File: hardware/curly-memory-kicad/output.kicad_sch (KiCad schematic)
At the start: 37 parts

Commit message: schematic updated with component fields on more components
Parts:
- C? (x12): footprint (none) -> Capacitor_SMD:C_0805_2012Metric_Pad1.18x1.45mm_HandSolder
- J? (x4): footprint (none) -> AudioJacks:Jack_3.5mm_QingPu_WQP-PJ398SM_Vertical
- R? (x12): footprint Resistor_THT:R_Axial_DIN0309_L9.0mm_D3.2mm_P12.70mm_Horizontal -> Resistor_SMD:R_0805_2012Metric_Pad1.20x1.40mm_HandSolder

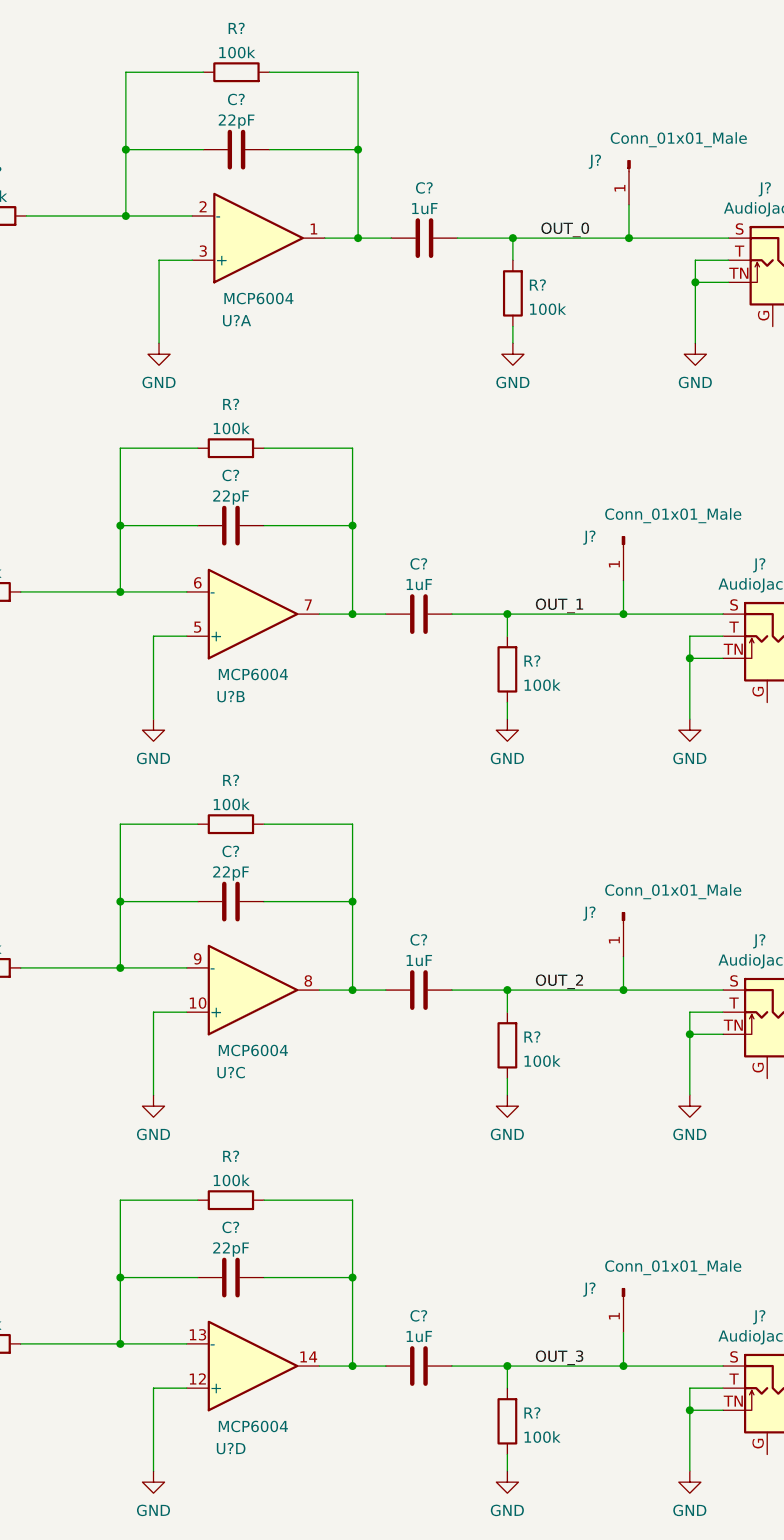
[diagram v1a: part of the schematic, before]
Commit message: all components have part numbers
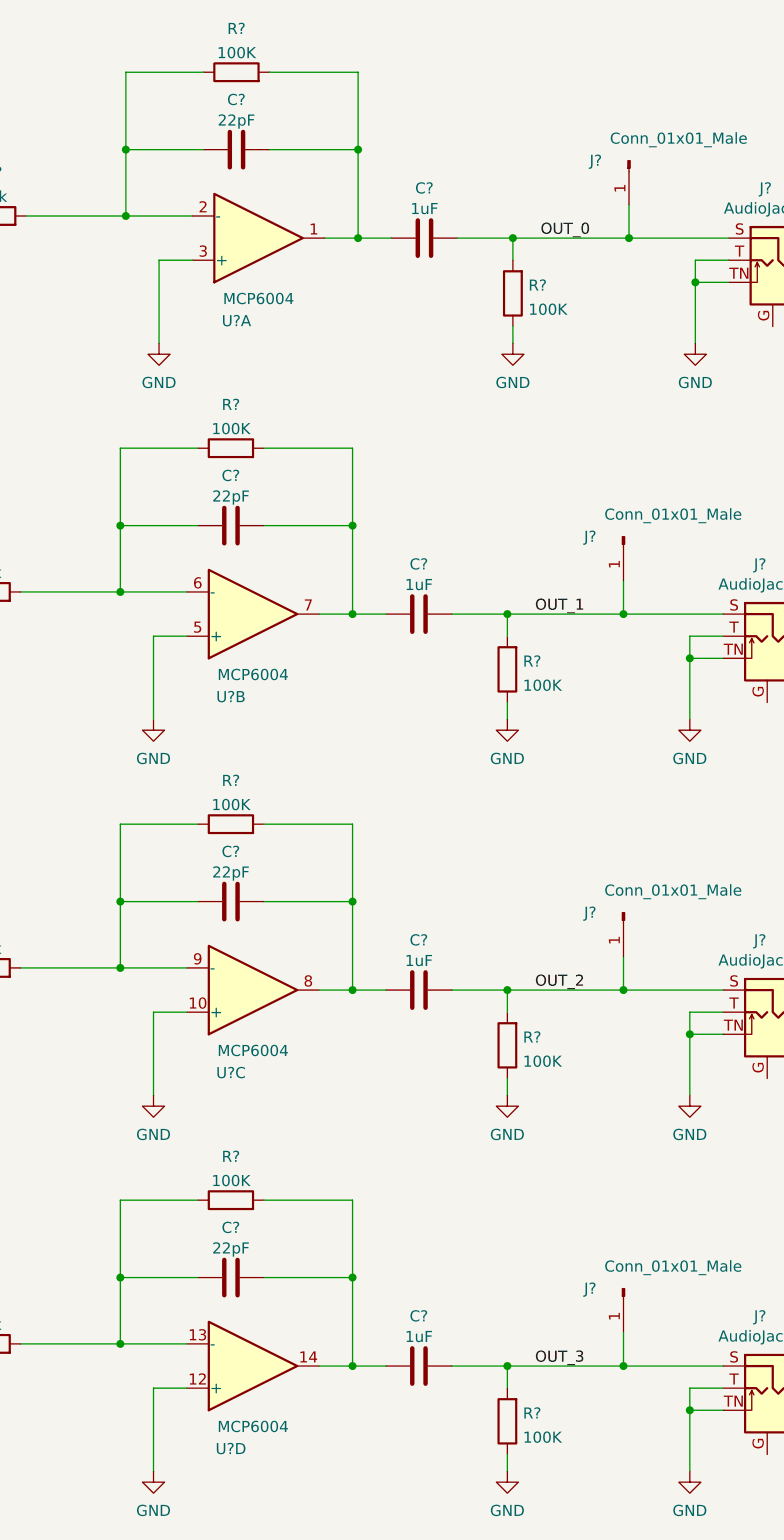
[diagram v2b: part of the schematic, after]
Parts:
- R? (x8): value 100k -> 100K
- U? (x5): footprint (none) -> Package_SO:SOIC-14_3.9x8.7mm_P1.27mm
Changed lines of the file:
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@@
     (in_bom yes) (on_board yes) (fields_autoplaced)
     (property "Reference" "R?" (id 0) (at 73.66 105.5075 90))
-    (property "Value" "100k" (id 1) (at 73.66 108.2826 90))
+    (property "Value" "100K" (id 1) (at 73.66 108.2826 90))
     (property "Footprint" "Resistor_SMD:R_0805_2012Metric_Pad1.20x1.40mm_HandSolder" (id 2) (at 73.66 112.268 90)
       (effects (font (size 1.27 1.27)) hide)
@@
       (effects (font (size 1.27 1.27)) (justify right))
     )
-    (property "Value" "100k" (id 1) (at 107.188 137.7566 0)
+    (property "Value" "100K" (id 1) (at 107.188 137.7566 0)
       (effects (font (size 1.27 1.27)) (justify right))
     )
@@
     (in_bom yes) (on_board yes) (fields_autoplaced)
     (property "Reference" "R?" (id 0) (at 74.295 19.1475 90))
-    (property "Value" "100k" (id 1) (at 74.295 21.9226 90))
+    (property "Value" "100K" (id 1) (at 74.295 21.9226 90))
     (property "Footprint" "Resistor_SMD:R_0805_2012Metric_Pad1.20x1.40mm_HandSolder" (id 2) (at 74.295 25.908 90)
       (effects (font (size 1.27 1.27)) hide)
@@
     (property "Reference" "U?" (id 0) (at 73.66 95.885 0))
     (property "Value" "MCP6004" (id 1) (at 76.2 93.345 0))
-    (property "Footprint" "" (id 2) (at 74.93 88.9 0)
+    (property "Footprint" "Package_SO:SOIC-14_3.9x8.7mm_P1.27mm" (id 2) (at 74.93 88.9 0)
       (effects (font (size 1.27 1.27)) hide)
     )
@@
     (in_bom yes) (on_board yes) (fields_autoplaced)
     (property "Reference" "R?" (id 0) (at 73.66 62.3275 90))
-    (property "Value" "100k" (id 1) (at 73.66 65.1026 90))
+    (property "Value" "100K" (id 1) (at 73.66 65.1026 90))
     (property "Footprint" "Resistor_SMD:R_0805_2012Metric_Pad1.20x1.40mm_HandSolder" (id 2) (at 73.66 69.088 90)
       (effects (font (size 1.27 1.27)) hide)
@@
     (property "Reference" "U?" (id 0) (at 73.66 182.245 0))
     (property "Value" "MCP6004" (id 1) (at 76.2 179.705 0))
-    (property "Footprint" "" (id 2) (at 74.93 175.26 0)
+    (property "Footprint" "Package_SO:SOIC-14_3.9x8.7mm_P1.27mm" (id 2) (at 74.93 175.26 0)
       (effects (font (size 1.27 1.27)) hide)
     )
@@
       (effects (font (size 1.27 1.27)) (justify right))
     )
-    (property "Value" "100k" (id 1) (at 107.188 94.5766 0)
+    (property "Value" "100K" (id 1) (at 107.188 94.5766 0)
       (effects (font (size 1.27 1.27)) (justify right))
     )
@@
       (effects (font (size 1.27 1.27)) (justify right))
     )
-    (property "Value" "100k" (id 1) (at 107.823 51.3966 0)
+    (property "Value" "100K" (id 1) (at 107.823 51.3966 0)
       (effects (font (size 1.27 1.27)) (justify right))
     )
@@
     (in_bom yes) (on_board yes) (fields_autoplaced)
     (property "Reference" "R?" (id 0) (at 73.66 148.6875 90))
-    (property "Value" "100k" (id 1) (at 73.66 151.4626 90))
+    (property "Value" "100K" (id 1) (at 73.66 151.4626 90))
     (property "Footprint" "Resistor_SMD:R_0805_2012Metric_Pad1.20x1.40mm_HandSolder" (id 2) (at 73.66 155.448 90)
       (effects (font (size 1.27 1.27)) hide)
@@
     (property "Reference" "U?" (id 0) (at 74.295 52.705 0))
     (property "Value" "MCP6004" (id 1) (at 76.835 50.165 0))
-    (property "Footprint" "" (id 2) (at 75.565 45.72 0)
+    (property "Footprint" "Package_SO:SOIC-14_3.9x8.7mm_P1.27mm" (id 2) (at 75.565 45.72 0)
       (effects (font (size 1.27 1.27)) hide)
     )
@@
     (property "Reference" "U?" (id 0) (at 73.66 139.065 0))
     (property "Value" "MCP6004" (id 1) (at 76.2 136.525 0))
-    (property "Footprint" "" (id 2) (at 74.93 132.08 0)
+    (property "Footprint" "Package_SO:SOIC-14_3.9x8.7mm_P1.27mm" (id 2) (at 74.93 132.08 0)
       (effects (font (size 1.27 1.27)) hide)
     )
@@
     (property "Reference" "U?" (id 0) (at 200.66 109.22 0))
     (property "Value" "MCP6004" (id 1) (at 182.88 109.22 0))
-    (property "Footprint" "" (id 2) (at 191.77 106.68 0)
+    (property "Footprint" "Package_SO:SOIC-14_3.9x8.7mm_P1.27mm" (id 2) (at 191.77 106.68 0)
       (effects (font (size 1.27 1.27)) hide)
     )
@@
       (effects (font (size 1.27 1.27)) (justify right))
     )
-    (property "Value" "100k" (id 1) (at 107.188 180.9366 0)
-      (effects (font (size 1.27 1.27)) (justify right))
-    )
+    (property "Value" "100K" (id 1) (at 107.188 180.9366 0)
+      (effects (font (size 1.27 1.27)) (justify right))
+    )
